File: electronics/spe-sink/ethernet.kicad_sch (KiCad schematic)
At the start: 30 parts, among them U4 ADIN1110, X1 RH100-25.000-13-F-0715

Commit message: Building out PDoE filter/isolation, etc
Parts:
- added C22: 220n_X7R_1005M, Applidyne_Capacitor:CAPC1005X60N, symbol appli_capacitor:220n_X7R_1005M
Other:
- note added: "10k2 resistor"
- note added: "49R9 resistor"
- note added: "5k1 resistor"
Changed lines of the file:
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@@
     (effects (font (size 1 1)) (justify left bottom))
+  )
+  (text "5k1 resistor" (at 87.63 38.1 0)
+    (effects (font (size 1.27 1.27)) (justify left bottom))
   )
   (text "LINK-UP" (at 16.51 121.92 0)
@@
     (effects (font (size 1 1)) (justify right bottom))
   )
+  (text "49R9 resistor" (at 88.9 24.13 0)
+    (effects (font (size 1.27 1.27)) (justify left bottom))
+  )
+  (text "10k2 resistor" (at 87.63 30.48 0)
+    (effects (font (size 1.27 1.27)) (justify left bottom))
+  )
   (text "DEFAULT: power-down" (at 91.44 171.45 0)
     (effects (font (size 1.27 1.27)) (justify left bottom))
@@
     (effects (font (size 1.27 1.27)) (justify left))
   )
+  (hierarchical_label "DATA+" (shape bidirectional) (at 36.83 43.18 180) (fields_autoplaced)
+    (effects (font (size 1.27 1.27)) (justify right))
+  )
   (hierarchical_label "{SPI}" (shape bidirectional) (at 229.87 101.6 0) (fields_autoplaced)
     (effects (font (size 1.27 1.27)) (justify left))
   )
-  (hierarchical_label "RXN" (shape input) (at 54.61 63.5 180) (fields_autoplaced)
-    (effects (font (size 1.27 1.27)) (justify right))
-  )
-  (hierarchical_label "TXP" (shape input) (at 54.61 58.42 180) (fields_autoplaced)
-    (effects (font (size 1.27 1.27)) (justify right))
-  )
-  (hierarchical_label "TXN" (shape input) (at 54.61 55.88 180) (fields_autoplaced)
+  (hierarchical_label "DATA-" (shape bidirectional) (at 36.83 38.1 180) (fields_autoplaced)
     (effects (font (size 1.27 1.27)) (justify right))
   )
   (hierarchical_label "~{INT}" (shape output) (at 255.27 97.79 0) (fields_autoplaced)
     (effects (font (size 1.27 1.27)) (justify left))
-  )
-  (hierarchical_label "RXP" (shape input) (at 54.61 60.96 180) (fields_autoplaced)
-    (effects (font (size 1.27 1.27)) (justify right))
   )
   (symbol (lib_id "appli_power:+3.3V") (at 187.96 21.59 0) (mirror y) (unit 1)
@@
         )
       )
+    )
+  )
+  (symbol (lib_id "appli_capacitor:220n_X7R_1005M") (at 60.96 38.1 90) (unit 1)
+    (in_bom yes) (on_board yes) (dnp no) (fields_autoplaced)
+    (property "Reference" "C22" (at 63.5 31.75 90)
+      (effects (font (size 1.27 1.27)))
+    )
+    (property "Value" "220n_X7R_1005M" (at 63.5 34.29 90)
+      (effects (font (size 0.889 0.889)))
+    )
+    (property "Footprint" "Applidyne_Capacitor:CAPC1005X60N" (at 63.5 35.179 90)
+      (effects (font (size 0.508 0.508)) hide)
+    )
+    (property "Datasheet" "http://www.yageo.com/documents/recent/UPY-GPHC_X7R_6.3V-to-50V_18.pdf" (at 63.5 34.544 90)
+      (effects (font (size 0.508 0.508)) hide)
+    )
+    (property "manf" "Yageo" (at 63.5 33.274 90)
+      (effects (font (size 0.508 0.508)) hide)
+    )
+    (property "manf#" "CC0402KRX7R9BB221" (at 63.5 32.639 90)
+      (effects (font (size 0.508 0.508)) hide)
+    )
+    (property "Supplier" "Digi-Key" (at 63.5 32.004 90)
+      (effects (font (size 0.508 0.508)) hide)
+    )
+    (property "Supplier Part No" "311-1035-1-ND" (at 63.5 31.369 90)
+      (effects (font (size 0.508 0.508)) hide)
+    )
+    (property "Supplier URL" "https://www.digikey.com.au/product-detail/en/yageo/CC0402KRX7R9BB221/311-1035-1-ND/302952" (at 63.5 30.734 90)
+      (effects (font (size 0.508 0.508)) hide)
+    )
+    (property "Supplier Price" "0.0186" (at 63.5 30.099 90)
+      (effects (font (size 0.508 0.508)) hide)
+    )
+    (property "Supplier Price Break" "100" (at 63.5 29.464 90)
+      (effects (font (size 0.508 0.508)) hide)
+    )
+    (pin "1")
+    (pin "2")
+    (instances
+      (project "spe-sink"
+        (path "/f0a501c7-1ad1-4c59-9255-3d6aa4545d8b/c444fd40-2442-4c73-bf48-a4aa084e5cc8"
+          (reference "C22") (unit 1)
+        )
+      )

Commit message: PD function board schematic progress
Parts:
- removed C22: 220n_X7R_1005M, Applidyne_Capacitor:CAPC1005X60N, symbol appli_capacitor:220n_X7R_1005M
- added R18, R25: 5K1_1005M, Applidyne_Resistor:RESC1005X40N, symbol appli_resistor:5K1_1005M
- added R20, R23: 10K2_1005M, Applidyne_Resistor:RESC1005X40N, symbol appli_resistor:10K2_1005M
- added R22, R24: 49R9_1005M, Applidyne_Resistor:RESC1005X40N, symbol appli_resistor:49R9_1005M
- C16, C17: footprint CAPC1608* -> Applidyne_Capacitor:CAPC1608X90N
- C7: footprint CAPC1005X60* -> Applidyne_Capacitor:CAPC1005X60N
- D1: footprint (none) -> Applidyne_LED:LEDC1608X80L40N
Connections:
- net DATA+: now also R24.1, R25.1
- net DATA-: now also R18.1, R22.1
- net at U4.12 (TXN): now also R22.2, R23.1
- net at U4.13 (RXN): now also R18.2, R20.1
- net at U4.14 (RXP): now also R23.2, R25.2
- net at U4.15 (TXP): now also R20.2, R24.2
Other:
- note added: "Blindly following ADIN1110 datasheet."
- note added: "External Hybrid Stage"
- note removed: "10k2 resistor"
- note removed: "49R9 resistor"
- note removed: "5k1 resistor"

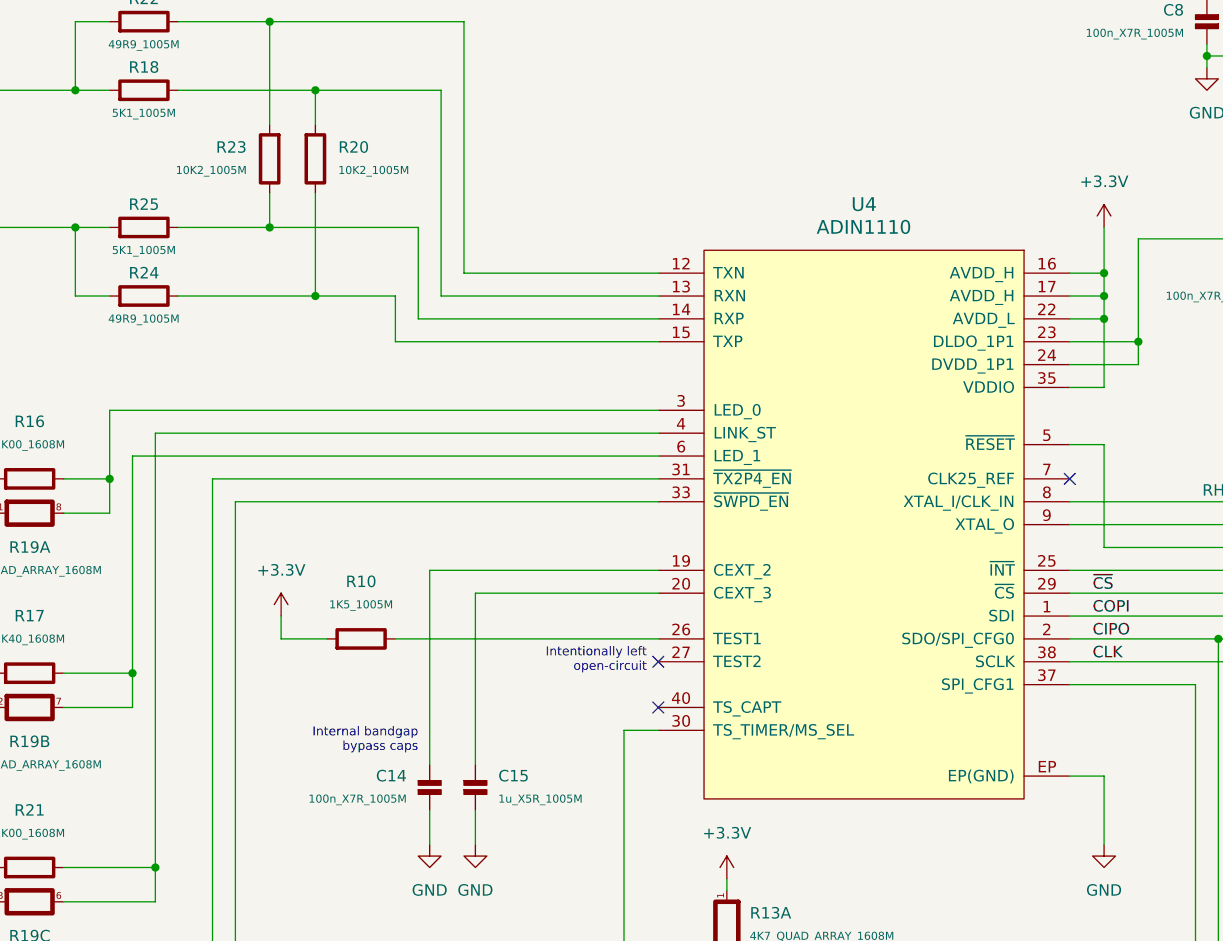
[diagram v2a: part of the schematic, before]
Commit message: PD function board bulk regulator, cleanup, part placement
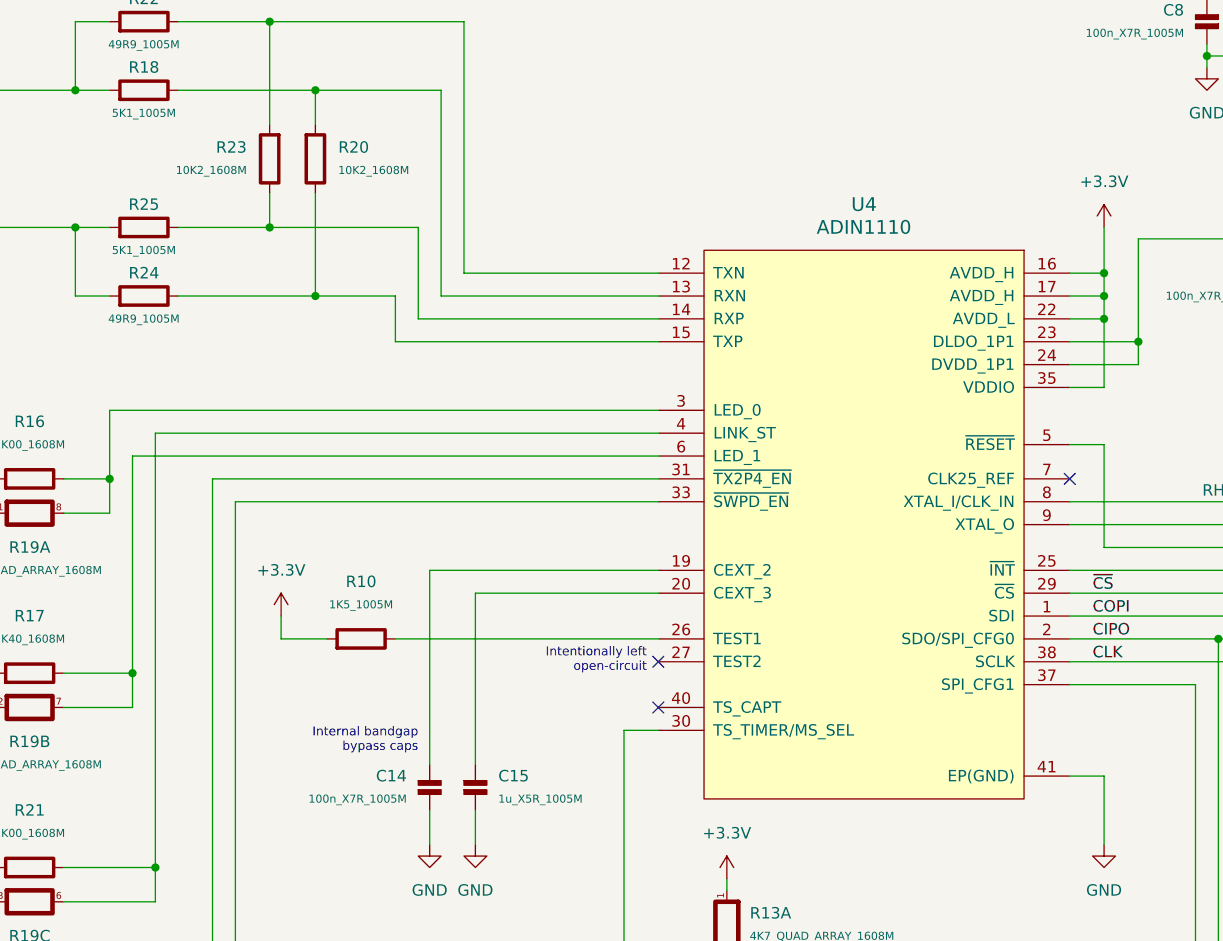
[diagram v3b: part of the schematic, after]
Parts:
- removed R20, R23: 10K2_1005M, Applidyne_Resistor:RESC1005X40N, symbol appli_resistor:10K2_1005M
- added R20, R23: 10K2_1608M, Applidyne_Resistor:RESC1608X50N, symbol appli_resistor:10K2_1608M
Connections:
- net GND: now also U4.41 (EP(GND)); no longer U4.EP (EP(GND))
- net at R18.2, U4.13 (RXN): now also R20.1
- net at R24.2, U4.15 (TXP): now also R20.2
- net at R25.2, U4.14 (RXP): now also R23.2
- net at R22.2, U4.12 (TXN): now also R23.1
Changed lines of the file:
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@@
-    )
-  )
-  (symbol (lib_id "appli_resistor:10K2_1005M") (at 88.9 39.37 0) (unit 1)
-    (in_bom yes) (on_board yes) (dnp no) (fields_autoplaced)
-    (property "Reference" "R20" (at 91.44 41.91 0)
-      (effects (font (size 1.27 1.27)) (justify left))
-    )
-    (property "Value" "10K2_1005M" (at 91.44 44.45 0)
-      (effects (font (size 0.889 0.889)) (justify left))
-    )
-    (property "Footprint" "Applidyne_Resistor:RESC1005X40N" (at 91.694 43.18 90)
-      (effects (font (size 0.508 0.508)) hide)
-    )
-    (property "Datasheet" "https://industrial.panasonic.com/cdbs/www-data/pdf/RDA0000/AOA0000C304.pdf" (at 92.329 43.18 90)
-      (effects (font (size 0.508 0.508)) hide)
-    )
-    (property "manf" "PANASONIC" (at 93.599 43.18 90)
-      (effects (font (size 0.508 0.508)) hide)
-    )
-    (property "manf#" "ERJ-2RKF1022X" (at 94.234 43.18 90)
-      (effects (font (size 0.508 0.508)) hide)
-    )
-    (property "Supplier" "Digikey" (at 94.869 43.18 90)
-      (effects (font (size 0.508 0.508)) hide)
-    )
-    (property "Supplier Part No" "P10.2KLCT-ND" (at 95.504 43.18 90)
-      (effects (font (size 0.508 0.508)) hide)
-    )
-    (property "Supplier URL" "https://www.digikey.com.au/en/products/detail/panasonic-electronic-components/ERJ-2RKF1022X/192075" (at 96.139 43.18 90)
-      (effects (font (size 0.508 0.508)) hide)
-    )
-    (property "Supplier Price" "0.018" (at 96.774 43.18 90)
-      (effects (font (size 0.508 0.508)) hide)
-    )
-    (property "Supplier Price Break" "100" (at 97.409 43.18 90)
-      (effects (font (size 0.508 0.508)) hide)
-    )
-    (pin "1")
-    (pin "2")
-    (instances
-      (project "spe-sink"
-        (path "/f0a501c7-1ad1-4c59-9255-3d6aa4545d8b/c444fd40-2442-4c73-bf48-a4aa084e5cc8"
-          (reference "R20") (unit 1)
-        )
-      )
     )
   )
@@
         (path "/f0a501c7-1ad1-4c59-9255-3d6aa4545d8b/c444fd40-2442-4c73-bf48-a4aa084e5cc8"
           (reference "C9") (unit 1)
+        )
+      )
+    )
+  )
+  (symbol (lib_id "appli_resistor:10K2_1608M") (at 83.82 39.37 0) (mirror y) (unit 1)
+    (in_bom yes) (on_board yes) (dnp no)
+    (property "Reference" "R23" (at 81.28 41.91 0)
+      (effects (font (size 1.27 1.27)) (justify left))
+    )
+    (property "Value" "10K2_1608M" (at 81.28 44.45 0)
+      (effects (font (size 0.889 0.889)) (justify left))
+    )
+    (property "Footprint" "Applidyne_Resistor:RESC1608X50N" (at 81.026 43.18 90)
+      (effects (font (size 0.508 0.508)) hide)
+    )
+    (property "Datasheet" "https://www.yageo.com/upload/media/product/productsearch/datasheet/rchip/PYu-RC_Group_51_RoHS_L_12.pdf" (at 80.391 43.18 90)
+      (effects (font (size 0.508 0.508)) hide)
+    )
+    (property "manf" "YAGEO" (at 79.121 43.18 90)
+      (effects (font (size 0.508 0.508)) hide)
+    )
+    (property "manf#" "RC0603FR-0710K2L" (at 78.486 43.18 90)
+      (effects (font (size 0.508 0.508)) hide)
+    )
+    (property "Supplier" "Digikey" (at 77.851 43.18 90)
+      (effects (font (size 0.508 0.508)) hide)
+    )
+    (property "Supplier Part No" "311-10.2KHRCT-ND" (at 77.216 43.18 90)
+      (effects (font (size 0.508 0.508)) hide)
+    )
+    (property "Supplier URL" "https://www.digikey.com.au/en/products/detail/yageo/RC0603FR-0710K2L/726883" (at 76.581 43.18 90)
+      (effects (font (size 0.508 0.508)) hide)
+    )
+    (property "Supplier Price" "0.02" (at 75.946 43.18 90)
+      (effects (font (size 0.508 0.508)) hide)
+    )
+    (property "Supplier Price Break" "10" (at 75.311 43.18 90)
+      (effects (font (size 0.508 0.508)) hide)
+    )
+    (pin "1")
+    (pin "2")
+    (instances
+      (project "spe-sink"
+        (path "/f0a501c7-1ad1-4c59-9255-3d6aa4545d8b/c444fd40-2442-4c73-bf48-a4aa084e5cc8"
+          (reference "R23") (unit 1)
         )
       )
@@
     (pin "4")
     (pin "40")
+    (pin "41")
     (pin "5")
     (pin "6")
@@
     (pin "8")
     (pin "9")
-    (pin "EP")
     (instances
       (project "spe-sink"
@@
     )
   )
-  (symbol (lib_id "appli_resistor:10K2_1005M") (at 83.82 39.37 0) (mirror y) (unit 1)
-    (in_bom yes) (on_board yes) (dnp no)
-    (property "Reference" "R23" (at 81.28 41.91 0)
-      (effects (font (size 1.27 1.27)) (justify left))
-    )
-    (property "Value" "10K2_1005M" (at 81.28 44.45 0)
-      (effects (font (size 0.889 0.889)) (justify left))
-    )
-    (property "Footprint" "Applidyne_Resistor:RESC1005X40N" (at 81.026 43.18 90)
-      (effects (font (size 0.508 0.508)) hide)
-    )
-    (property "Datasheet" "https://industrial.panasonic.com/cdbs/www-data/pdf/RDA0000/AOA0000C304.pdf" (at 80.391 43.18 90)
-      (effects (font (size 0.508 0.508)) hide)
-    )
-    (property "manf" "PANASONIC" (at 79.121 43.18 90)
-      (effects (font (size 0.508 0.508)) hide)
-    )
-    (property "manf#" "ERJ-2RKF1022X" (at 78.486 43.18 90)
-      (effects (font (size 0.508 0.508)) hide)
-    )
-    (property "Supplier" "Digikey" (at 77.851 43.18 90)
-      (effects (font (size 0.508 0.508)) hide)
-    )
-    (property "Supplier Part No" "P10.2KLCT-ND" (at 77.216 43.18 90)
-      (effects (font (size 0.508 0.508)) hide)
-    )
-    (property "Supplier URL" "https://www.digikey.com.au/en/products/detail/panasonic-electronic-components/ERJ-2RKF1022X/192075" (at 76.581 43.18 90)
-      (effects (font (size 0.508 0.508)) hide)
-    )
-    (property "Supplier Price" "0.018" (at 75.946 43.18 90)
-      (effects (font (size 0.508 0.508)) hide)
-    )
-    (property "Supplier Price Break" "100" (at 75.311 43.18 90)
-      (effects (font (size 0.508 0.508)) hide)
-    )
-    (pin "1")
-    (pin "2")
-    (instances
-      (project "spe-sink"
-        (path "/f0a501c7-1ad1-4c59-9255-3d6aa4545d8b/c444fd40-2442-4c73-bf48-a4aa084e5cc8"
-          (reference "R23") (unit 1)
-        )
-      )
-    )
-  )
   (symbol (lib_id "appli_link:SOLDER-LINK-2-TINY") (at 68.58 163.83 270) (mirror x) (unit 1)
     (in_bom yes) (on_board yes) (dnp no)
@@
         )
       )
+    )
+  )
+  (symbol (lib_id "appli_resistor:10K2_1608M") (at 88.9 39.37 0) (unit 1)
+    (in_bom yes) (on_board yes) (dnp no) (fields_autoplaced)
+    (property "Reference" "R20" (at 91.44 41.91 0)
+      (effects (font (size 1.27 1.27)) (justify left))
+    )
+    (property "Value" "10K2_1608M" (at 91.44 44.45 0)
+      (effects (font (size 0.889 0.889)) (justify left))
+    )
+    (property "Footprint" "Applidyne_Resistor:RESC1608X50N" (at 91.694 43.18 90)
+      (effects (font (size 0.508 0.508)) hide)
+    )
+    (property "Datasheet" "https://www.yageo.com/upload/media/product/productsearch/datasheet/rchip/PYu-RC_Group_51_RoHS_L_12.pdf" (at 92.329 43.18 90)
+      (effects (font (size 0.508 0.508)) hide)
+    )
+    (property "manf" "YAGEO" (at 93.599 43.18 90)
+      (effects (font (size 0.508 0.508)) hide)
+    )
+    (property "manf#" "RC0603FR-0710K2L" (at 94.234 43.18 90)
+      (effects (font (size 0.508 0.508)) hide)
+    )
+    (property "Supplier" "Digikey" (at 94.869 43.18 90)
+      (effects (font (size 0.508 0.508)) hide)
+    )
+    (property "Supplier Part No" "311-10.2KHRCT-ND" (at 95.504 43.18 90)
+      (effects (font (size 0.508 0.508)) hide)
+    )
+    (property "Supplier URL" "https://www.digikey.com.au/en/products/detail/yageo/RC0603FR-0710K2L/726883" (at 96.139 43.18 90)
+      (effects (font (size 0.508 0.508)) hide)
+    )
+    (property "Supplier Price" "0.02" (at 96.774 43.18 90)
+      (effects (font (size 0.508 0.508)) hide)
+    )
+    (property "Supplier Price Break" "10" (at 97.409 43.18 90)
+      (effects (font (size 0.508 0.508)) hide)
+    )
+    (pin "1")
+    (pin "2")
+    (instances
+      (project "spe-sink"
+        (path "/f0a501c7-1ad1-4c59-9255-3d6aa4545d8b/c444fd40-2442-4c73-bf48-a4aa084e5cc8"
+          (reference "R20") (unit 1)
+        )
+      )

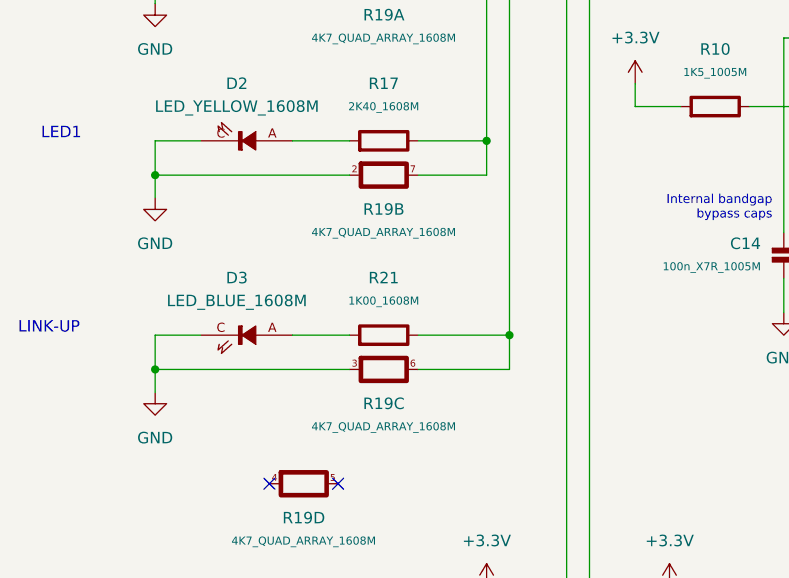
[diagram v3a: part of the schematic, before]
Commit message: PD sink board routing, minor sch changes, etc
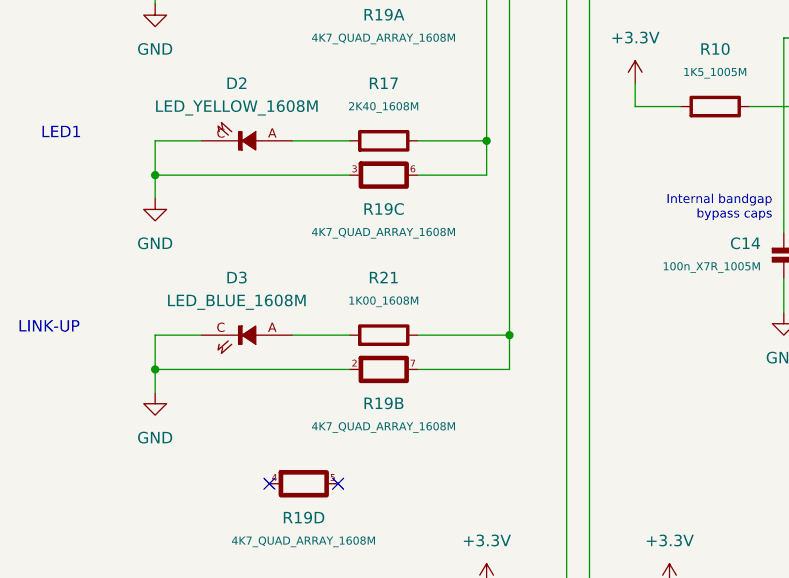
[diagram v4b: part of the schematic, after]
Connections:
- net GND: now also R19.2, R19.3; no longer R19.2, R19.3
- net at R17.2, U4.6 (LED_1): now also R19.6; no longer R19.7
- net at R21.2, U4.4 (LINK_ST): now also R19.7; no longer R19.6
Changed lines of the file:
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@@
     )
   )
-  (symbol (lib_id "appli_resistor:4K7_QUAD_ARRAY_1608M") (at 53.34 104.14 90) (unit 2)
+  (symbol (lib_id "appli_resistor:4K7_QUAD_ARRAY_1608M") (at 53.34 104.14 90) (unit 3)
     (in_bom yes) (on_board yes) (dnp no)
     (property "Reference" "R19" (at 57.15 107.95 90)
@@
       (project "spe-sink"
         (path "/f0a501c7-1ad1-4c59-9255-3d6aa4545d8b/c444fd40-2442-4c73-bf48-a4aa084e5cc8"
-          (reference "R19") (unit 2)
+          (reference "R19") (unit 3)
         )
       )
@@
     )
   )
-  (symbol (lib_id "appli_resistor:4K7_QUAD_ARRAY_1608M") (at 53.34 125.73 90) (unit 3)
+  (symbol (lib_id "appli_resistor:4K7_QUAD_ARRAY_1608M") (at 53.34 125.73 90) (unit 2)
     (in_bom yes) (on_board yes) (dnp no)
     (property "Reference" "R19" (at 57.15 129.54 90)
@@
       (project "spe-sink"
         (path "/f0a501c7-1ad1-4c59-9255-3d6aa4545d8b/c444fd40-2442-4c73-bf48-a4aa084e5cc8"
-          (reference "R19") (unit 3)
-        )
-      )
+          (reference "R19") (unit 2)
+        )
+      )
